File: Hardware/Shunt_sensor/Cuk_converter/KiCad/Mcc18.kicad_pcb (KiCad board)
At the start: 2 copper layers, 199.2 x 138.3 mm, 61 parts, among them Q1 IRFP4321PbF, U1 INA240, U2 DRIVER_(INEP), U3 LM7812_TO220, U4 Signals_MCC, U5 ZCS

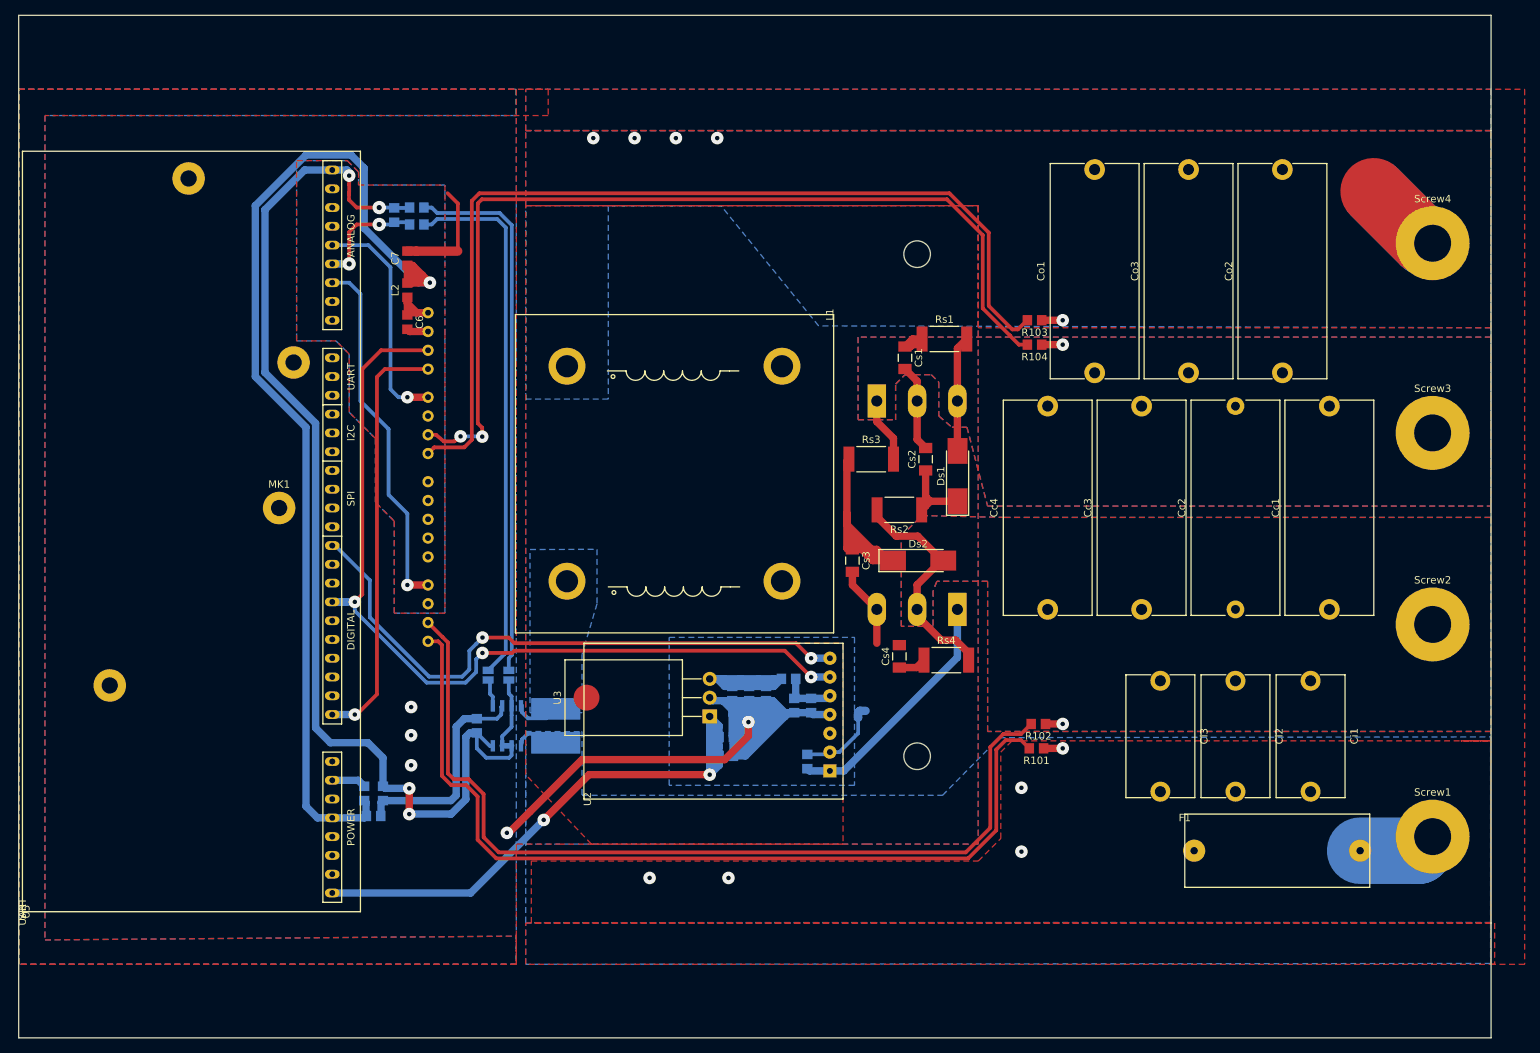
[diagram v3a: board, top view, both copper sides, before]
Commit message: Copper Clearence fixed
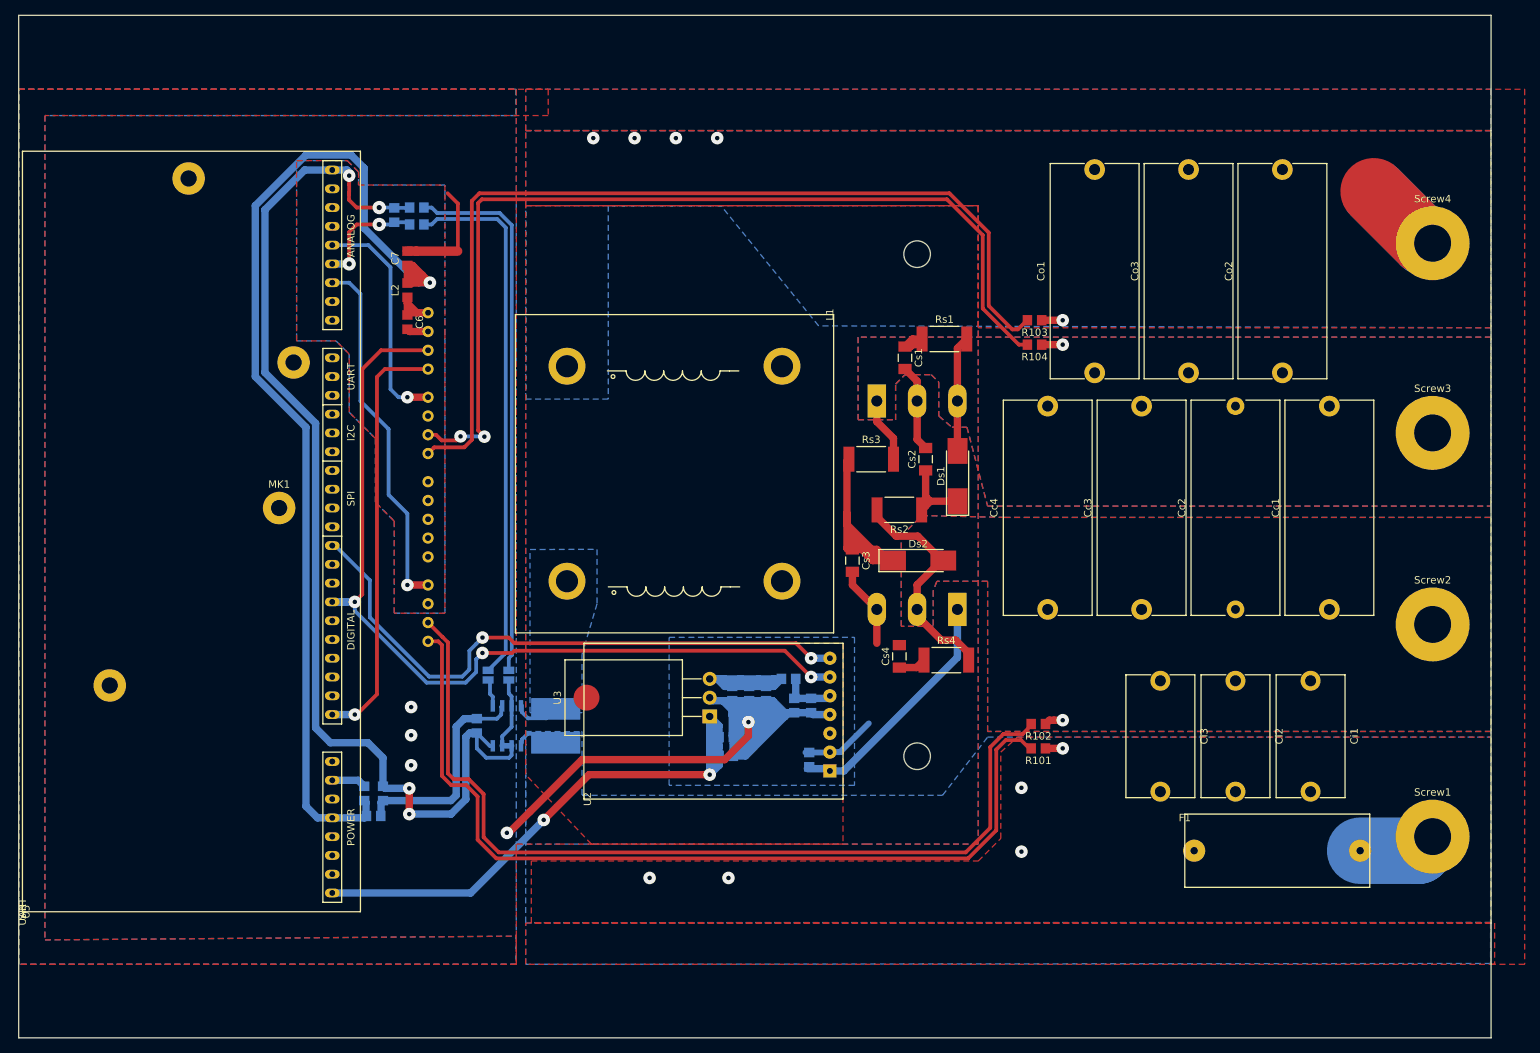
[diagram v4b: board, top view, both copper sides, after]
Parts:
- moved R1 0.36 mm to (157.0, 125.0)
- moved R101 0.25 mm to (188.0, 123.4)
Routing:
- net /Source: track 35.7 -> 34.4 mm

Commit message: finalized shunt cuk
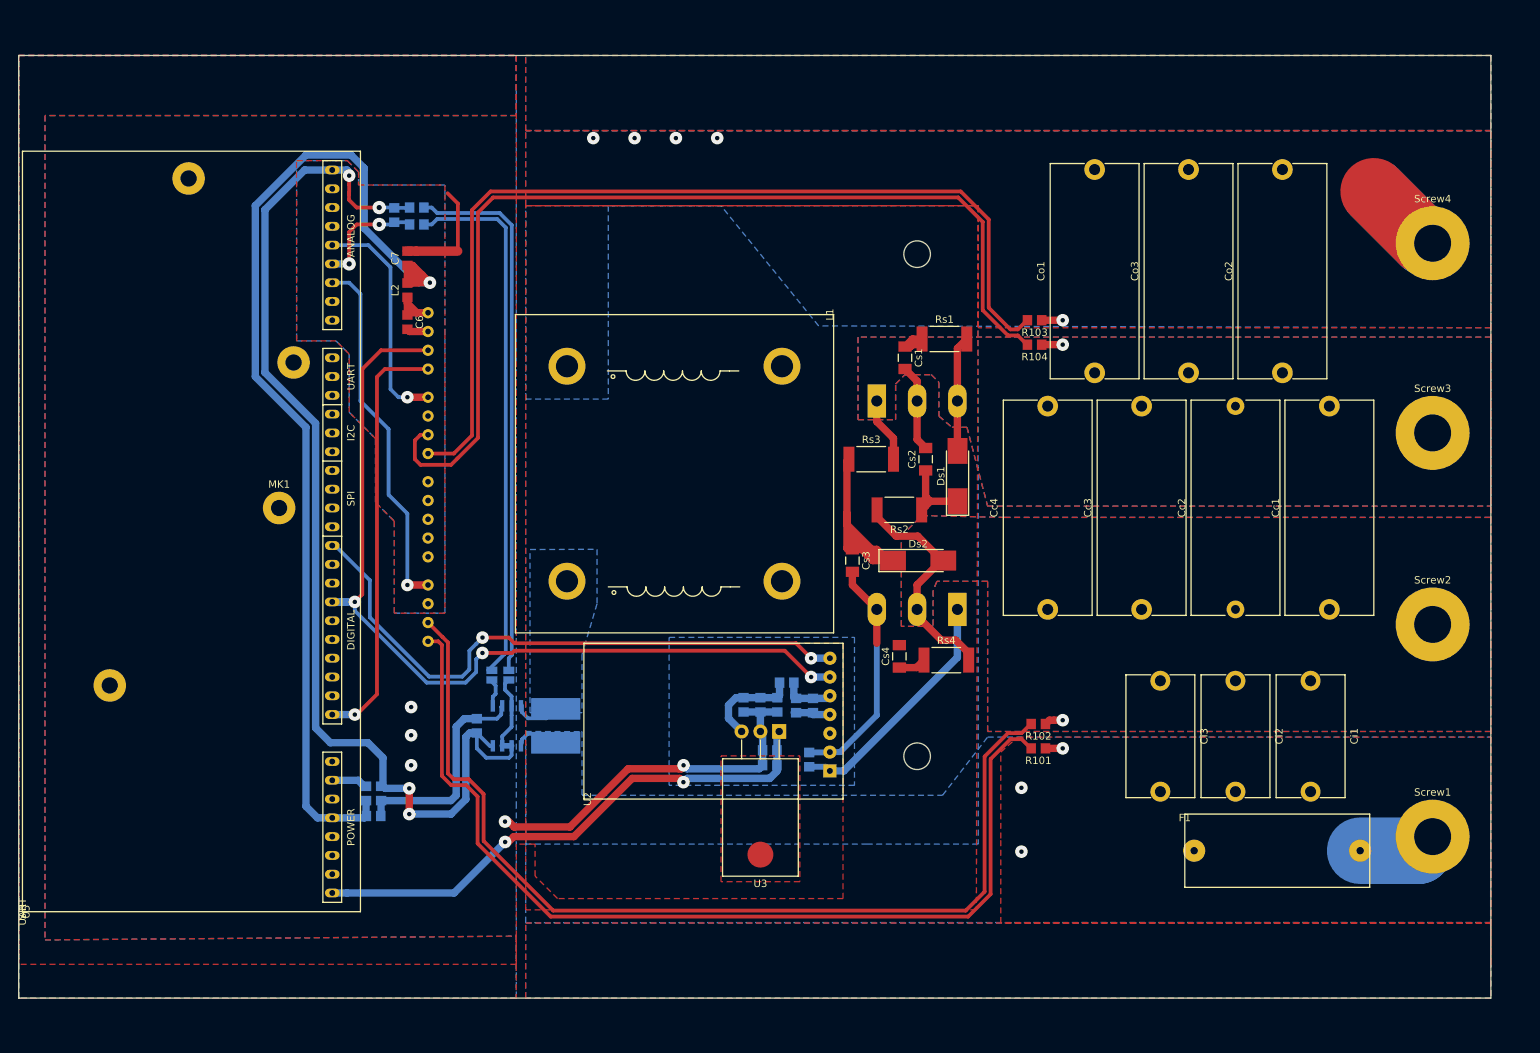
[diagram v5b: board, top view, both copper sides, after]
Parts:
- moved U3 9.62 mm to (152.9, 121.2), turned to 180 degrees
- moved C3 7.02 mm to (151.6, 125.7), turned to 180 degrees
- moved C2 5.94 mm to (151.6, 123.7), turned to 180 degrees
- moved C13 2.29 mm to (99.1, 129.5)
- moved C12 2.29 mm to (97.0, 129.5)
- moved C4 2.16 mm to (148.1, 117.6)
- moved C5 2.16 mm to (150.4, 117.6)
- moved C8 2.16 mm to (152.7, 117.6)
- moved L3 0.57 mm to (153.9, 114.6)
- moved R105 0.51 mm to (114.0, 113.5)
- moved C10 0.25 mm to (155.2, 117.7)
- moved C9 0.25 mm to (157.5, 117.7)
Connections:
- C12 pad 1: Net-(C11-Pad2) -> +5V
- C12 pad 2: GNDA -> GND
- C13 pad 1: +5V -> Net-(C11-Pad2)
- C13 pad 2: GND -> GNDA
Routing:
- net GND: track 241.8 -> 158.1 mm
- net +12V: track 29.9 -> 13.5 mm
- net /Source: track 34.4 -> 49.8 mm
- net /Vp_sen-: track 121.5 -> 133.0 mm
- net /Vp_sen+: track 122.0 -> 133.2 mm
- net /+18V_OUT: track 84.0 -> 72.9 mm
- net /Vb_sen-: track 128.7 -> 135.9 mm, vias 2 -> 0
- net /-Vp: vias 5 -> 3
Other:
- board size 199.2 x 138.3 mm -> 199.1 x 127.5 mm
